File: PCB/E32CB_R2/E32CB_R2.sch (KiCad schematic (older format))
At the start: 82 parts, among them J1 GND, J10 VM1, J11 GND, J12 VM2, J13 GND, J14 P3B, J15 GND, J16 P3A, J17 NEXTION, J18 Power, J19 OneWire, J2 pump, J20 I2C, J21 USB_B, J3 GND, J4 LED, J5 GND, J6 P12B, J7 GND, J8 P12A, J9 GND, Q1 S8050, Q10 IRLR2905, Q2 S8050, Q3 IRLR2905, Q4 IRLR2905, Q5 IRLR2905, Q6 IRLR2905, Q7 IRLR2905, Q8 IRLR2905, Q9 IRLR2905, U1 ESP32-WROOM-32, X1 12MHz

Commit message: rename and update
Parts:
- removed R1: 4k7, Resistor_SMD:R_0805_2012Metric_Pad1.15x1.40mm_HandSolder, symbol Device:R_Small

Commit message: schema update
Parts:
- C6, C7, C8, C9: symbol Device:C -> Device:C_Small
- renumbered LED_R to LED_R1, LED_R to LED_R2, LED_R to LED_R3, LED_R to LED_R4, sw_push to sw_push1, sw_push to sw_push2
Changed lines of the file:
@@
 	7500 2800 7450 2800
 $Comp
-L Device:C C7
+L Device:C_Small C7
 U 1 1 5DF1AC2C
 P 7850 3100
@@
 	8350 3100 8350 3350
 Wire Wire Line
-	7850 3250 7850 3350
-Wire Wire Line
-	7850 2950 7850 2800
-Wire Wire Line
-	8850 3350 8850 3250
-Wire Wire Line
 	8650 2800 8850 2800
-Wire Wire Line
-	8850 2800 8850 2950
 $Comp
 L power:+3V3 #PWR045
@@
 $EndComp
 $Comp
-L Device:C C6
+L Device:C_Small C6
 U 1 1 5DEFEA91
 P 7650 1550
@@
 $EndComp
 $Comp
-L Device:C C8
+L Device:C_Small C8
 U 1 1 5DF004CD
 P 8650 1550
@@
 	8450 1250 8650 1250
 Wire Wire Line
-	8650 1250 8650 1400
-Wire Wire Line
 	7850 1250 7650 1250
-Wire Wire Line
-	7650 1250 7650 1400
 $Comp
 L power:+12V #PWR035
@@
 	11000 900  11000 1350
 $Comp
-L Device:LED LED_R
+L Device:LED LED_R1
 U 1 1 5E04BA83
 P 3500 3800
-F 0 "LED_R" H 3493 3545 50  0000 C CNN
+F 0 "LED_R1" H 3493 3545 50  0000 C CNN
 F 1 "RXD" H 3493 3636 50  0000 C CNN
 F 2 "Mlab_D:LED_1206" H 3500 3800 50  0001 C CNN
@@
 $EndComp
 $Comp
-L Device:LED LED_R
+L Device:LED LED_R2
 U 1 1 5E062710
 P 3500 4150
-F 0 "LED_R" H 3500 3900 50  0000 C CNN
+F 0 "LED_R2" H 3500 3900 50  0000 C CNN
 F 1 "TXD" H 3493 3986 50  0000 C CNN
 F 2 "Mlab_D:LED_1206" H 3500 4150 50  0001 C CNN
@@
 TXD
 $Comp
-L Device:LED LED_R
+L Device:LED LED_R3
 U 1 1 5E08E5BB
 P 3500 4550
-F 0 "LED_R" H 3500 4300 50  0000 C CNN
+F 0 "LED_R3" H 3500 4300 50  0000 C CNN
 F 1 "Power" H 3493 4386 50  0000 C CNN
 F 2 "Mlab_D:LED_1206" H 3500 4550 50  0001 C CNN
@@
 $EndComp
 $Comp
-L Device:LED LED_R
+L Device:LED LED_R4
 U 1 1 5E08F438
 P 3500 4950
-F 0 "LED_R" H 3500 4700 50  0000 C CNN
+F 0 "LED_R4" H 3500 4700 50  0000 C CNN
 F 1 "Signal" H 3493 4786 50  0000 C CNN
 F 2 "Mlab_D:LED_1206" H 3500 4950 50  0001 C CNN
@@
 	3650 5850 3750 5850
 $Comp
-L Switch:SW_Push sw_push
+L Switch:SW_Push sw_push1
 U 1 1 5E140153
 P 3450 5850
-F 0 "sw_push" H 3450 6043 50  0001 C CNN
+F 0 "sw_push1" H 3450 6043 50  0001 C CNN
 F 1 "RESET" H 3450 6044 50  0000 C CNN
 F 2 "Buttons_Switches_THT:SW_PUSH_6mm_h4.3mm" H 3450 6050 50  0001 C CNN
@@
 	3650 6150 3750 6150
 $Comp
-L Switch:SW_Push sw_push
+L Switch:SW_Push sw_push2
 U 1 1 5E1870C9
 P 3450 6150
-F 0 "sw_push" H 3450 6343 50  0001 C CNN
+F 0 "sw_push2" H 3450 6343 50  0001 C CNN
 F 1 "MODE" H 3450 6344 50  0000 C CNN
 F 2 "Buttons_Switches_THT:SW_PUSH_6mm_h4.3mm" H 3450 6350 50  0001 C CNN
@@
 	1    0    0    -1
 $EndComp
-Wire Wire Line
-	8650 1700 8650 1800
-Wire Wire Line
-	7650 1700 7650 1800
 $Comp
 L Device:R_Small R19
@@
 	8050 2800 7850 2800
 $Comp
-L Device:C C9
+L Device:C_Small C9
 U 1 1 5E1CB6EF
 P 8850 3100
@@
 	0    1    1    0
 $EndComp
+Wire Wire Line
+	7650 1250 7650 1450
+Wire Wire Line
+	7650 1650 7650 1800
+Wire Wire Line
+	8650 1250 8650 1450
+Wire Wire Line
+	8650 1650 8650 1800
+Wire Wire Line
+	7850 2800 7850 3000
+Wire Wire Line
+	7850 3200 7850 3350
+Wire Wire Line
+	8850 3200 8850 3350
+Wire Wire Line
+	8850 2800 8850 3000
 $EndSCHEMATC

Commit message: pcb schema update
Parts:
- added D3: 1N4007, Diode_SMD:D_SMA_Handsoldering, symbol Diode:1N4007
- added J22: USB +5V, Mlab_Pin_Headers:Straight_2x03, symbol MLAB_HEADER:HEADER_2x03_PARALLEL
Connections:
- net +12V: now also D3.2 (A); no longer 3V3stabilizer1.1 (VI), C7.1, D2.1 (K)
- net +5V: now also J22.3, J22.4
- net GND: now also J22.1, J22.2, J22.5, J22.6
- new net: 3V3stabilizer1.1 (VI), C7.1, D2.1 (K), D3.1 (K)
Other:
- note added: "USB +5V"
- moved on the sheet: C7, C9, D2

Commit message: USB voltage distribution
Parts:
- C9: footprint Capacitor_SMD:C_0805_2012Metric_Pad1.15x1.40mm_HandSolder -> Capacitors_SMD:C_0805_HandSoldering
- D2, D3: footprint Diode_SMD:D_SMA_Handsoldering -> Diodes_SMD:D_SMA_Handsoldering
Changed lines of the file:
@@
 F 0 "D2" H 7650 2800 50  0000 C CNN
 F 1 "1N4007" H 7700 3000 50  0000 C CNN
-F 2 "Diode_SMD:D_SMA_Handsoldering" H 7650 2725 50  0001 C CNN
+F 2 "Diodes_SMD:D_SMA_Handsoldering" H 7650 2725 50  0001 C CNN
 F 3 "http://www.vishay.com/docs/88503/1n4001.pdf" H 7650 2900 50  0001 C CNN
 	1    7650 2900
@@
 F 0 "C9" H 8965 3246 50  0000 L CNN
 F 1 "2.2uF" H 8965 3155 50  0000 L CNN
-F 2 "Capacitor_SMD:C_0805_2012Metric_Pad1.15x1.40mm_HandSolder" H 8888 3050 50  0001 C CNN
+F 2 "Capacitors_SMD:C_0805_HandSoldering" H 8888 3050 50  0001 C CNN
 F 3 "~" H 8850 3200 50  0001 C CNN
 	1    8850 3200
@@
 F 0 "D3" H 7850 2500 50  0000 C CNN
 F 1 "1N4007" H 7900 2700 50  0000 C CNN
-F 2 "Diode_SMD:D_SMA_Handsoldering" H 7850 2425 50  0001 C CNN
+F 2 "Diodes_SMD:D_SMA_Handsoldering" H 7850 2425 50  0001 C CNN
 F 3 "http://www.vishay.com/docs/88503/1n4001.pdf" H 7850 2600 50  0001 C CNN
 	1    7850 2600
@@
 $EndComp
 $Comp
-L power:+5V #PWR?
+L power:+5V #PWR0101
 U 1 1 5E579F4B
 P 3400 6150
-F 0 "#PWR?" H 3400 6000 50  0001 C CNN
+F 0 "#PWR0101" H 3400 6000 50  0001 C CNN
 F 1 "+5V" H 3415 6323 50  0000 C CNN
 F 2 "" H 3400 6150 50  0001 C CNN
@@
 $EndComp
 $Comp
-L power:GND #PWR?
+L power:GND #PWR0102
 U 1 1 5E57A61F
 P 3550 6250
-F 0 "#PWR?" H 3550 6000 50  0001 C CNN
+F 0 "#PWR0102" H 3550 6000 50  0001 C CNN
 F 1 "GND" H 3555 6077 50  0000 C CNN
 F 2 "" H 3550 6250 50  0001 C CNN
@@
 $EndComp
 $Comp
-L power:GND #PWR?
+L power:GND #PWR0103
 U 1 1 5E57AFB5
 P 3250 6250
-F 0 "#PWR?" H 3250 6000 50  0001 C CNN
+F 0 "#PWR0103" H 3250 6000 50  0001 C CNN
 F 1 "GND" H 3255 6077 50  0000 C CNN
 F 2 "" H 3250 6250 50  0001 C CNN

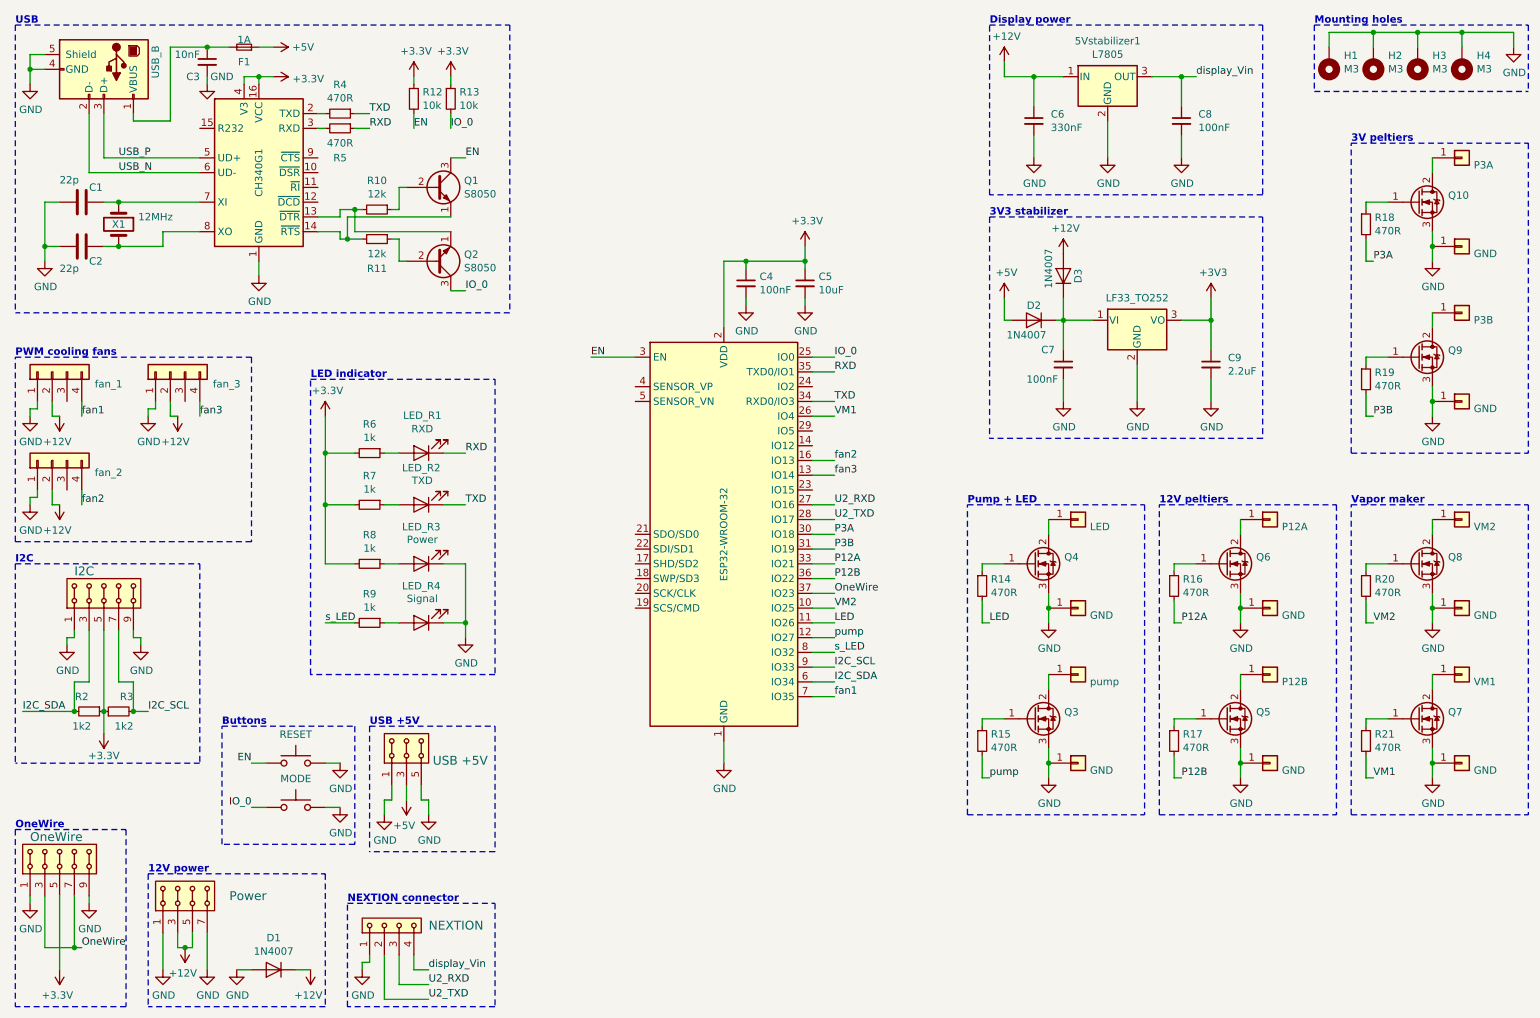
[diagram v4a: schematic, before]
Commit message: esp pin update, pin header added
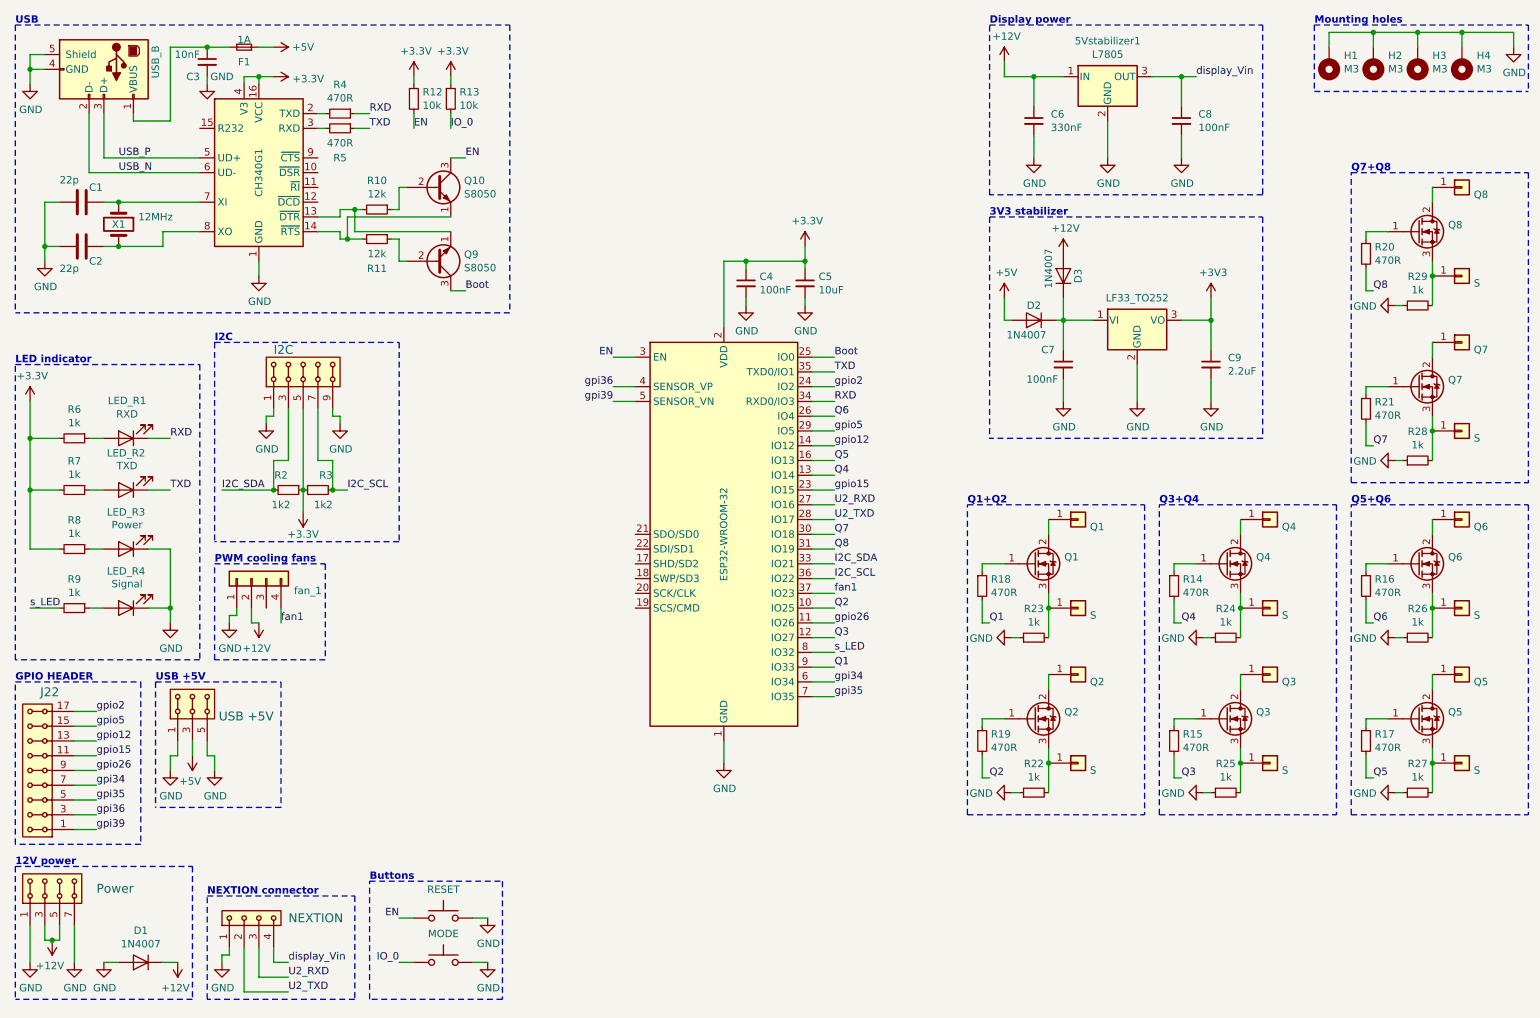
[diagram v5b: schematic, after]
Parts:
- removed J19: OneWire, Mlab_Pin_Headers:Straight_2x05, symbol MLAB_HEADER:HEADER_2x05_PARALLEL
- removed fan_2, fan_3: Conn_01x04, Connector:FanPinHeader_1x04_P2.54mm_Vertical, symbol Connector_Generic:Conn_01x04
- added J22: GPIO_HEADER, Mlab_Pin_Headers:Straight_2x09, symbol MLAB_HEADER:HEADER_2x09_PARALLEL
- added R22, R23, R24, R25, R26, R27, R28, R29: 1k, Resistors_SMD:R_0805_HandSoldering, symbol Device:R_Small
- J1, J11, J13, J15, J3, J5, J7, J9: value GND -> S
- J10: value VM1 -> Q7
- J12: value VM2 -> Q8
- J14: value P3B -> Q2
- J16: value P3A -> Q1
- J2: value pump -> Q3
- J4: value LED -> Q4
- J6: value P12B -> Q5
- J8: value P12A -> Q6
- renumbered Q10 to Q1, Q1 to Q10, Q9 to Q2, Q2 to Q9
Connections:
- net OneWire is gone; now on net fan1: U1.37 (IO23)
- net fan2 is gone; now on net Q5: U1.16 (IO13)
- net fan3 is gone; now on net Q4: U1.13 (IO14)
- net GND: now also R22.1, R23.1, R24.1, R25.1, R26.1, R27.1, R28.1, R29.1; no longer J1.1 (Pin_1), J11.1 (Pin_1), J13.1 (Pin_1), J15.1 (Pin_1), J3.1 (Pin_1), J5.1 (Pin_1), J7.1 (Pin_1), J9.1 (Pin_1), Q1.3 (S), Q2.3 (S), Q3.3 (S), Q4.3 (S), Q5.3 (S), Q6.3 (S), Q7.3 (S), Q8.3 (S)
- net I2C_SCL: now also U1.36 (IO22); no longer U1.9 (IO33)
- net I2C_SDA: now also U1.33 (IO21); no longer U1.6 (IO34)
- net IO_0: no longer Q9.3 (C), U1.25 (IO0)
- net RXD: now also R4.1, U1.34 (RXD0/IO3); no longer R5.1, U1.35 (TXD0/IO1)
- net TXD: now also R5.1, U1.35 (TXD0/IO1); no longer R4.1, U1.34 (RXD0/IO3)
- net fan1: no longer U1.7 (IO35)
- net gpio12: now reaches U1.14 (IO12)
- net gpio12: now also J22.13, J22.14
- net gpio15: now reaches U1.23 (IO15)
- net gpio15: now also J22.11, J22.12
- net gpio2: now reaches U1.24 (IO2)
- net gpio2: now also J22.17, J22.18
- net gpio5: now reaches U1.29 (IO5)
- net gpio5: now also J22.15, J22.16
- net gpi36: now reaches U1.4 (SENSOR_VP)
- net gpi36: now also J22.3, J22.4
- net gpi39: now reaches U1.5 (SENSOR_VN)
- net gpi39: now also J22.1, J22.2
- net LED renamed Q4
- net Q4: no longer U1.11 (IO26)
- net P12A renamed Q6
- net Q6: now also U1.26 (IO4); no longer U1.33 (IO21)
- net P12B renamed Q5
- net Q5: no longer U1.36 (IO22)
- net P3A renamed Q1
- net Q1: now also U1.9 (IO33); no longer U1.30 (IO18)
- net P3B renamed Q2
- net Q2: now also U1.10 (IO25); no longer U1.31 (IO19)
- net VM1 renamed Q7
- net Q7: now also U1.30 (IO18); no longer U1.26 (IO4)
- net VM2 renamed Q8
- net Q8: now also U1.31 (IO19); no longer U1.10 (IO25)
- net pump renamed Q3
- new net: J15.1 (Pin_1), Q1.3 (S), R23.2
- new net: J13.1 (Pin_1), Q2.3 (S), R22.2
- new net: J11.1 (Pin_1), Q8.3 (S), R29.2
- new net: J9.1 (Pin_1), Q7.3 (S), R28.2
- new net: J7.1 (Pin_1), Q6.3 (S), R26.2
- new net: J5.1 (Pin_1), Q5.3 (S), R27.2
- new net: J3.1 (Pin_1), Q4.3 (S), R24.2
- new net: J1.1 (Pin_1), Q3.3 (S), R25.2
- new net Boot: Q9.3 (C), U1.25 (IO0)
- new net gpi34: J22.7, J22.8, U1.6 (IO34)
- new net gpi35: J22.5, J22.6, U1.7 (IO35)
- new net gpio26: J22.10, J22.9, U1.11 (IO26)
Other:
- note added: "GPIO HEADER"
- note added: "Q1+Q2"
- note added: "Q3+Q4"
- note added: "Q5+Q6"
- note added: "Q7+Q8"
- note removed: "12V peltiers"
- note removed: "3V peltiers"
- note removed: "OneWire"
- note removed: "Pump + LED"
- note removed: "Vapor maker"
- moved on the sheet: D1, LED_R1, LED_R2, LED_R3, LED_R4, Q1, Q2, Q3, Q4, Q5, Q6, Q7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

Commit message: pcb update
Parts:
- C1, C2, C3, C6, C9: footprint Capacitors_SMD:C_0805_HandSoldering -> Capacitor_SMD:C_0805_2012Metric_Pad1.15x1.40mm_HandSolder
- C7: renamed from C8; footprint Capacitors_SMD:C_0805_HandSoldering -> Capacitor_SMD:C_0805_2012Metric_Pad1.15x1.40mm_HandSolder
- D1, D2, D3: footprint Diodes_SMD:D_SMA_Handsoldering -> Diode_SMD:D_MELF_Handsoldering
- Q1: renamed from Q10; footprint TO_SOT_Packages_SMD:SOT-23 -> Package_TO_SOT_SMD:SOT-23
- Q2: renamed from Q9; footprint TO_SOT_Packages_SMD:SOT-23 -> Package_TO_SOT_SMD:SOT-23
- R15: renamed from R23; footprint Resistors_SMD:R_0805_HandSoldering -> Resistor_SMD:R_0805_2012Metric_Pad1.15x1.40mm_HandSolder
- R16: renamed from R22; footprint Resistors_SMD:R_0805_HandSoldering -> Resistor_SMD:R_0805_2012Metric_Pad1.15x1.40mm_HandSolder
- R19: renamed from R24; footprint Resistors_SMD:R_0805_HandSoldering -> Resistor_SMD:R_0805_2012Metric_Pad1.15x1.40mm_HandSolder
- R20: renamed from R25; footprint Resistors_SMD:R_0805_HandSoldering -> Resistor_SMD:R_0805_2012Metric_Pad1.15x1.40mm_HandSolder
- R25: renamed from R29; footprint Resistors_SMD:R_0805_HandSoldering -> Resistor_SMD:R_0805_2012Metric_Pad1.15x1.40mm_HandSolder
- R26: renamed from R28; footprint Resistors_SMD:R_0805_HandSoldering -> Resistor_SMD:R_0805_2012Metric_Pad1.15x1.40mm_HandSolder
- R27: renamed from R26; footprint Resistors_SMD:R_0805_HandSoldering -> Resistor_SMD:R_0805_2012Metric_Pad1.15x1.40mm_HandSolder
- R28: renamed from R27; footprint Resistors_SMD:R_0805_HandSoldering -> Resistor_SMD:R_0805_2012Metric_Pad1.15x1.40mm_HandSolder
- U1: symbol RF_Module:ESP32-WROOM-32 -> E32CB_R2-rescue:ESP32-WROOM-32-RF_Module
- X1: footprint Crystals:Crystal_SMD_HC49-SD_HandSoldering -> Crystal:Crystal_SMD_HC49-SD_HandSoldering
- sw_push1, sw_push2: footprint Buttons_Switches_THT:SW_PUSH_6mm_h4.3mm -> Button_Switch_THT:SW_PUSH_6mm
- renumbered C7 to C8, J22 to J1, J13 to J10, J4 to J11, J3 to J12, J2 to J13, J1 to J14, J12 to J15, J11 to J16, J10 to J17, J9 to J18, J8 to J19, J18 to J2, J7 to J20, J6 to J21, J5 to J22, J21 to J3, J22 to J4, J17 to J5, J20 to J6, J16 to J7, J15 to J8, J14 to J9, Q5 to Q10, Q1 to Q3, Q2 to Q4, Q4 to Q5, Q3 to Q6, Q8 to Q7, Q7 to Q8, Q6 to Q9, R6 to R1, R11 to R10, R12 to R11, R13 to R12, R18 to R13, R19 to R14, R14 to R17, R15 to R18, R7 to R2, R20 to R21, R21 to R22, R16 to R23, R17 to R24, R8 to R3, R9 to R4, R2 to R5, R3 to R6, R4 to R7, R5 to R8, R10 to R9

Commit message: pcb delete
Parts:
- removed U1: ESP32-WROOM-32, RF_Module:ESP32-WROOM-32, symbol E32CB_R2-rescue:ESP32-WROOM-32-RF_Module
- added U1: ESP32-WROOM-32, RF_Module:ESP32-WROOM-32, symbol RF_Module:ESP32-WROOM-32
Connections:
- net +3V3: now also U1.2 (VDD)
- net Boot: now also U1.25 (IO0)
- net EN: now also U1.3 (EN)
- net GND: now also U1.1 (GND), U1.15 (GND), U1.38 (GND), U1.39 (GND)
- net I2C_SCL: now also U1.36 (IO22)
- net I2C_SDA: now also U1.33 (IO21)
- net Q1: now also U1.9 (IO33)
- net Q2: now also U1.10 (IO25)
- net Q3: now also U1.12 (IO27)
- net Q4: now also U1.13 (IO14)
- net Q5: now also U1.16 (IO13)
- net Q6: now also U1.26 (IO4)
- net Q7: now also U1.30 (IO18)
- net Q8: now also U1.31 (IO19)
- net RXD: now also U1.34 (RXD0/IO3)
- net TXD: now also U1.35 (TXD0/IO1)
- net U2_RXD: now also U1.27 (IO16)
- net U2_TXD: now also U1.28 (IO17)
- net fan1: now also U1.37 (IO23)
- net gpi34: now also U1.6 (IO34)
- net gpi35: now also U1.7 (IO35)
- net gpi36: now also U1.4 (SENSOR_VP)
- net gpi39: now also U1.5 (SENSOR_VN)
- net gpio12: now also U1.14 (IO12)
- net gpio15: now also U1.23 (IO15)
- net gpio2: now also U1.24 (IO2)
- net gpio26: now also U1.11 (IO26)
- net gpio5: now also U1.29 (IO5)
- net s_LED: now also U1.8 (IO32)
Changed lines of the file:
@@
 EESchema Schematic File Version 4
-LIBS:E32CB_R2-cache
 EELAYER 26 0
 EELAYER END
@@
 	1    2500 1250
 	0    1    1    0
-$EndComp
-$Comp
-L E32CB_R2-rescue:ESP32-WROOM-32-RF_Module U1
-U 1 1 5DA32DFA
-P 5550 4350
-F 0 "U1" H 5550 5931 50  0001 C CNN
-F 1 "ESP32-WROOM-32" V 5550 4350 50  0000 C CNN
-F 2 "RF_Module:ESP32-WROOM-32" H 5550 2850 50  0001 C CNN
-F 3 "https://www.espressif.com/sites/default/files/documentation/esp32-wroom-32_datasheet_en.pdf" H 5250 4400 50  0001 C CNN
-	1    5550 4350
-	1    0    0    -1
 $EndComp
 $Comp
@@
 Text Notes 750  5350 0    50   ~ 10
 GPIO HEADER
+$Comp
+L RF_Module:ESP32-WROOM-32 U1
+U 1 1 5E9AC344
+P 5550 4350
+F 0 "U1" V 5550 5928 50  0001 C CNN
+F 1 "ESP32-WROOM-32" V 5550 4150 50  0000 C CNN
+F 2 "RF_Module:ESP32-WROOM-32" H 5550 2850 50  0001 C CNN
+F 3 "https://www.espressif.com/sites/default/files/documentation/esp32-wroom-32_datasheet_en.pdf" H 5250 4400 50  0001 C CNN
+	1    5550 4350
+	1    0    0    -1
+$EndComp
 $EndSCHEMATC

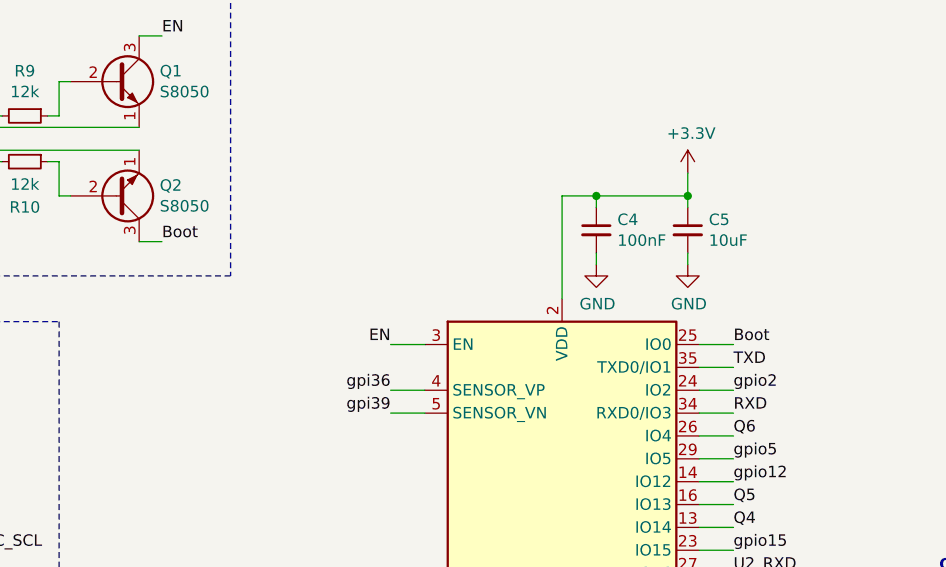
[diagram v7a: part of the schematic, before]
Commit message: reset section
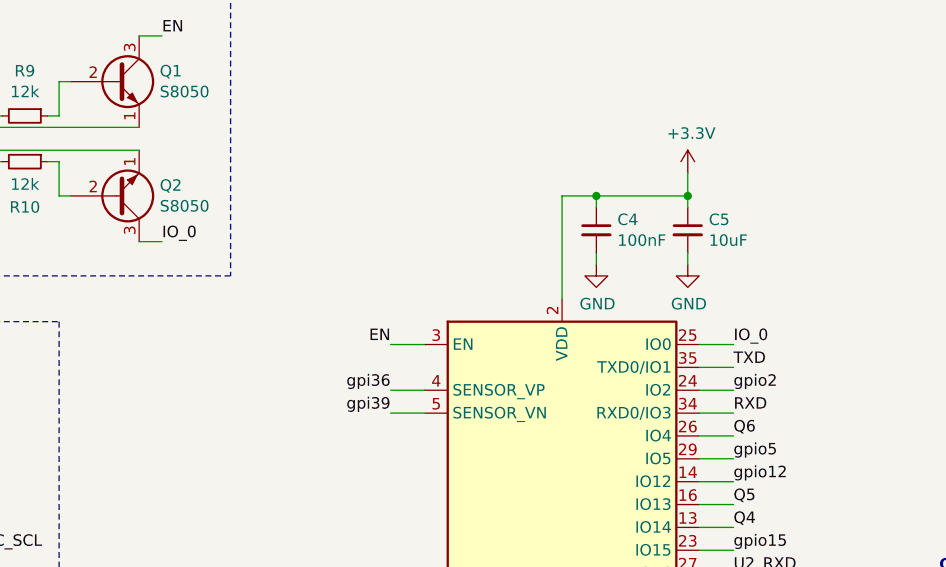
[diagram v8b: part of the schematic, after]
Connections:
- net Boot is gone; now on net IO_0: Q2.3 (C), U1.25 (IO0)
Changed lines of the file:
@@
 EESchema Schematic File Version 4
+LIBS:E32CB_R2-cache
 EELAYER 26 0
 EELAYER END
@@
 EN
 Text Label 6300 3150 0    50   ~ 0
-Boot
+IO_0
 $Comp
 L power:+3.3V #PWR029
@@
 EN
 Text Label 3800 2700 0    50   ~ 0
-Boot
+IO_0
 $Comp
 L power:+3.3V #PWR023
